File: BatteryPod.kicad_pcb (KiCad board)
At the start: 2 copper layers, 71.5 x 86.6 mm, 24 parts, among them J1 VIN, U1 LM5157RTER

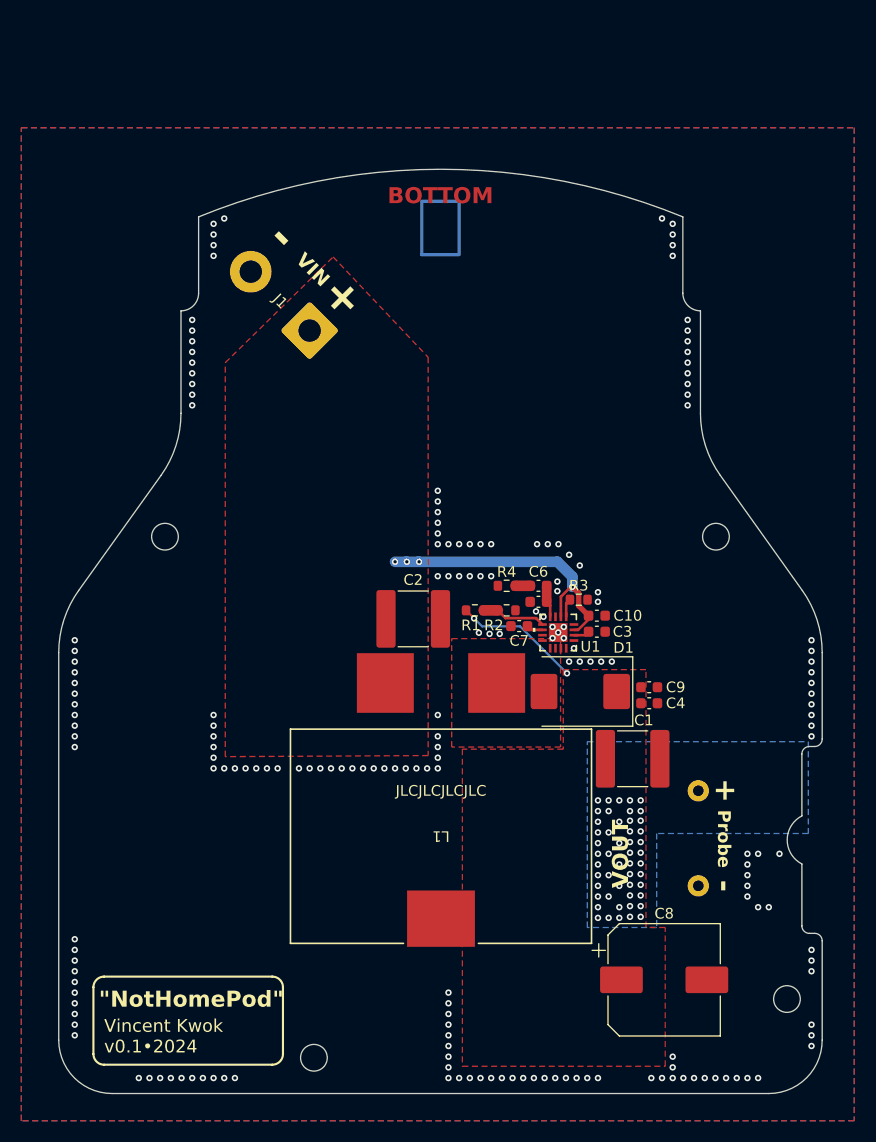
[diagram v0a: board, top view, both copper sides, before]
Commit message: feat: add partial USB-PD input, routing
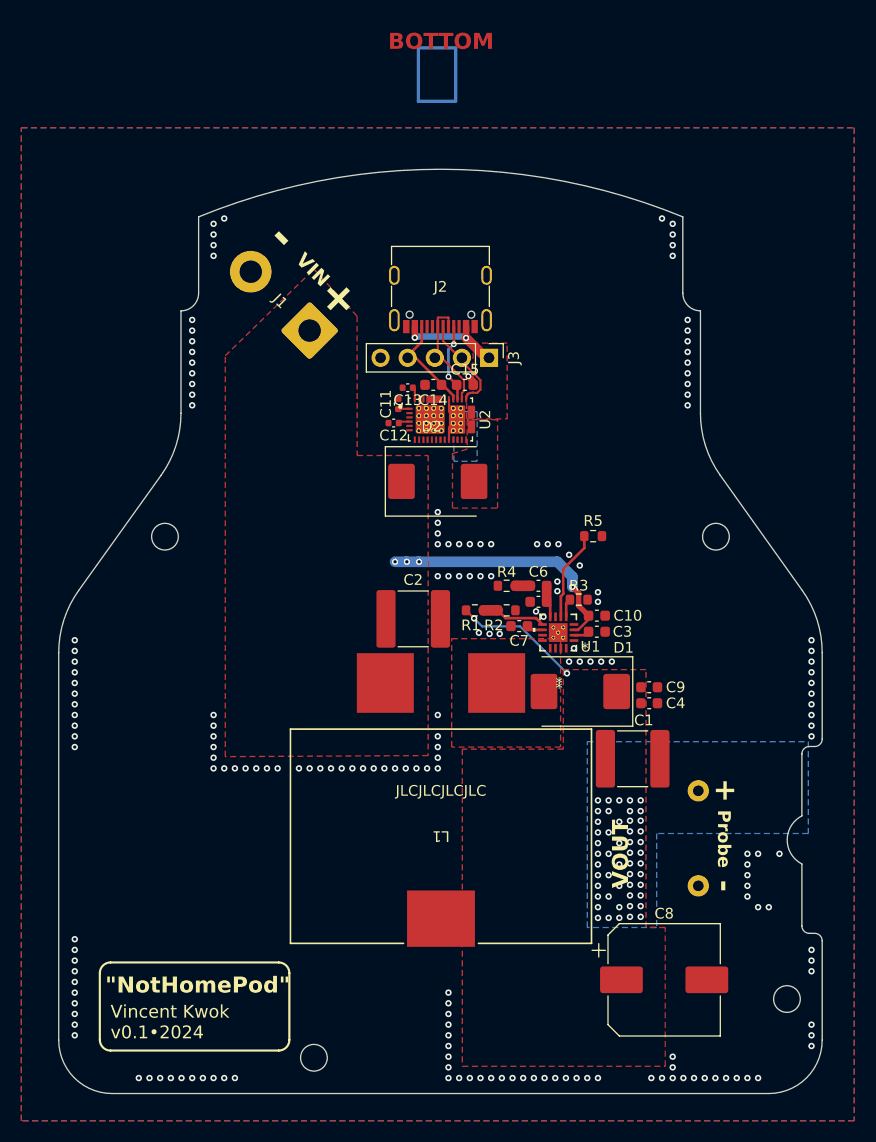
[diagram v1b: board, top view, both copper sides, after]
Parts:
- added C11: 10uF, Capacitor_SMD:C_0402_1005Metric, F.Cu at (106.3, 88.9)
- added C12: 10uF, Capacitor_SMD:C_0402_1005Metric, F.Cu at (105.9, 90.7)
- added C13: 10uF, Capacitor_SMD:C_0402_1005Metric, F.Cu at (107.2, 87.3)
- added C14: 300pF, Capacitor_SMD:C_0603_1608Metric, F.Cu at (109.6, 87.1)
- added C15: 300pF, Capacitor_SMD:C_0603_1608Metric, F.Cu at (112.5, 87.1)
- added D2: B3100-13-F, Diode_SMD:D_SMC, F.Cu at (110.0, 96.1)
- added J2: USB_C_Receptacle_USB2.0_16P, Connector_USB:USB_C_Receptacle_G-Switch_GT-USB-7010ASV, F.Cu at (110.2, 77.9)
- added J3: Conn_01x05_Pin, Connector_PinHeader_2.54mm:PinHeader_1x05_P2.54mm_Vertical, F.Cu at (114.8, 84.5)
- added R5: 2.49K, Resistor_SMD:R_0603_1608Metric, F.Cu at (124.5, 101.2)
- added U2: TPS25750DRJKR, Ti:IC_TPS25750DRJKR, F.Cu at (110.2, 90.3)
- D1: value D_Schottky -> B3100-13-F
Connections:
- U1 pad 6: +BATT -> /REG_EN
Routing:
- net /USB PD/DN: track 0.00 -> 10.6 mm
- net /USB PD/CC2: track 0.00 -> 9.82 mm
- net /USB PD/VBUS: track 0.00 -> 9.73 mm, vias 0 -> 2
- net /USB PD/DP: track 0.00 -> 9.13 mm
- net /REG_EN: track 0.00 -> 8.41 mm
- net /USB PD/CC1: track 0.00 -> 7.35 mm, vias 0 -> 2
- net Net-(U2-DRAIN): track 0.00 -> 3.53 mm
- net +BATT: track 26.9 -> 23.7 mm
- net Net-(U2-VIN_3V3): track 0.00 -> 1.12 mm
- net Net-(U2-LDO_3V3): track 0.00 -> 1.11 mm
- net Net-(U2-LDO_1V5): track 0.00 -> 1.00 mm
- net GND: track 0.00 -> 0.99 mm, vias 192 -> 186
- added copper zone on F.Cu, net /USB PD/VBUS
- added copper zone on F.Cu, net Net-(D2-A)
- added copper zone on B.Cu, net Net-(U2-DRAIN)
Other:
- rule pad_to_mask_clearance: 0 -> 0.038

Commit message: feat: fully routed USB-PD, new lower profile inductor
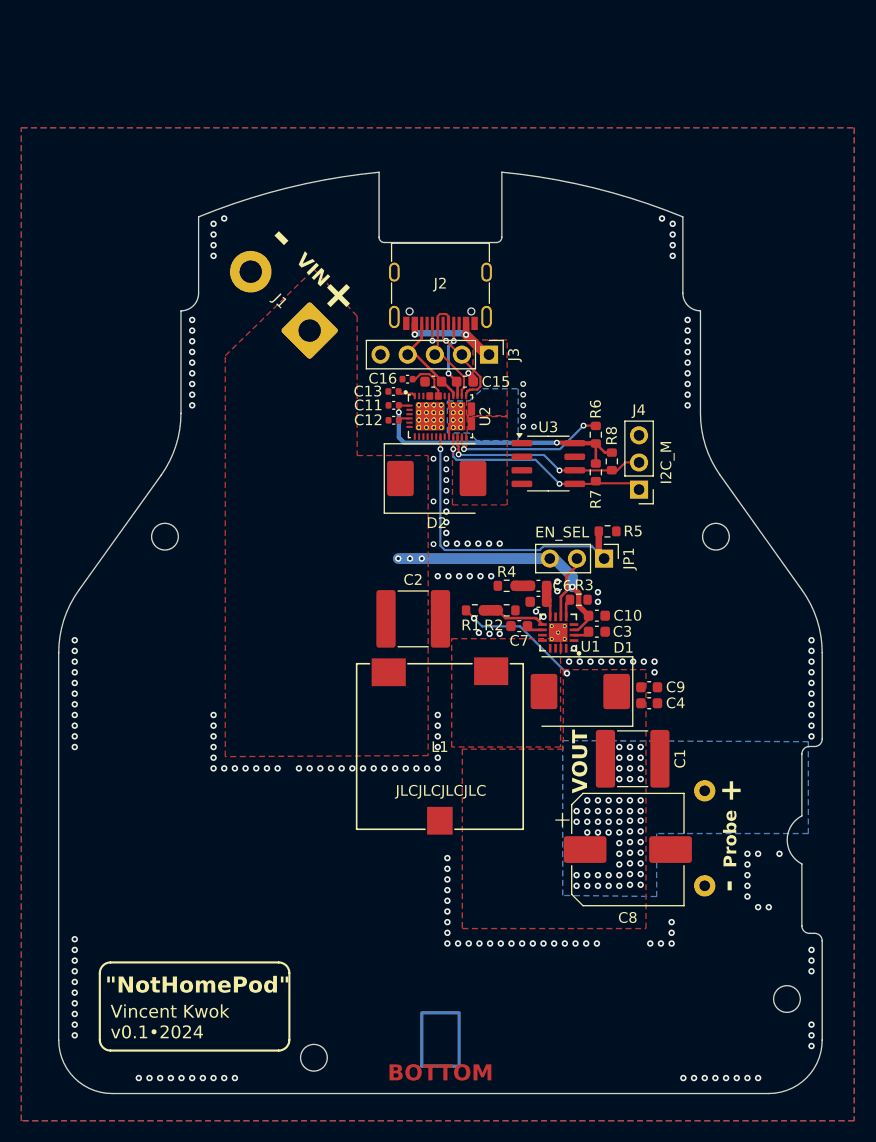
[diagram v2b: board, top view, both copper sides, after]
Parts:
- added C16: 10uF, Capacitor_SMD:C_0402_1005Metric, F.Cu at (107.2, 86.5)
- added J4: I2C_M, Connector_PinHeader_2.54mm:PinHeader_1x03_P2.54mm_Vertical, F.Cu at (128.8, 96.9)
- added JP1: EN_SEL, Connector_PinHeader_2.54mm:PinHeader_1x03_P2.54mm_Vertical, F.Cu at (125.6, 103.3)
- added R6: 2.49K, Resistor_SMD:R_0603_1608Metric, F.Cu at (124.8, 91.8)
- added R7: 2.49K, Resistor_SMD:R_0603_1608Metric, F.Cu at (124.8, 95.3)
- added R8: 2.49K, Resistor_SMD:R_0603_1608Metric, F.Cu at (126.3, 94.2)
- added U3: CAT24C256, Package_SO:SOIC-8_3.9x4.9mm_P1.27mm, F.Cu at (120.3, 94.5)
- L1: value SER2918H-333KL -> CDEP15D90T150NP-220MC; footprint coilcraft-ser2918h:IND_SER2918H_COC -> Sumida:CDEP15D90T150NP-220MC
- R4: value 63.4K -> 1.21K
- moved C8 12.7 mm to (127.8, 130.6)
- moved L1 8.36 mm to (110.2, 121.0)
- moved R5 1.42 mm to (125.9, 100.8)
- moved C13 1.38 mm to (105.8, 87.7)
- moved TP1 0.60 mm to (135.0, 125.1)
- moved TP2 0.60 mm to (135.0, 134.0)
- moved C11 0.45 mm to (105.9, 89.0), turned to 180 degrees
- moved J2 0.30 mm to (110.2, 77.6)
- moved C14 0.30 mm to (109.6, 86.8)
- moved C15 0.30 mm to (112.5, 86.8)
- moved J3 0.30 mm to (114.8, 84.2)
- moved U2 0.30 mm to (110.2, 90.0)
- moved D2 0.29 mm to (109.9, 95.8)
- moved C12 0.26 mm to (105.9, 90.4)
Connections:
- net Net-(U2-LDO_3V3) renamed /USB PD/LDO_3V3
- R5 pad 1: /REG_EN -> /PD_READY
- U2 pad 13: unconnected-(U2-GPIO11-Pad13) -> /PD_READY
- U2 pad 19: /REG_EN -> unconnected-(U2-GPIO3-Pad19)
- U2 pad 32_33: unconnected-(U2-VBUS-Pad32_33) -> Net-(U2-VBUS)
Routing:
- net /PD_READY: track 0.00 -> 28.4 mm, vias 0 -> 1
- net /USB PD/LDO_3V3: track 1.11 -> 26.5 mm, vias 0 -> 2
- net /USB PD/I2C_SDA: track 0.00 -> 20.8 mm, vias 0 -> 2
- net /USB PD/I2C_SCL: track 0.00 -> 19.5 mm, vias 0 -> 2
- net /USB PD/I2C_IRQ: track 0.00 -> 14.5 mm, vias 0 -> 2
- net Net-(U2-VBUS): track 0.00 -> 4.25 mm
- net /USB PD/DP: track 9.13 -> 12.0 mm, vias 0 -> 2
- net /REG_EN: track 8.41 -> 6.08 mm
- net Net-(U2-VIN_3V3): track 1.12 -> 1.70 mm
- net VCC: vias 52 -> 63
- net GND: vias 186 -> 201
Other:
- board size 71.5 x 86.6 mm -> 71.5 x 86.3 mm
- board text added: "USB PD"

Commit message: patch: final trace cleaups/parameter updates
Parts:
- C3: value 0.1uF -> 1uF
- moved C9 2.15 mm to (129.0, 113.4), turned to 90 degrees
- moved C4 1.20 mm to (129.7, 115.7)
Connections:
- U1 pad 15: unconnected-(U1-NC-Pad15) -> GND
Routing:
- net GND: vias 201 -> 200
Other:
- outline, holes or cut-outs redrawn
- rule pad_to_mask_clearance: 0.038 -> 0
- board text added: "Min 60W"
